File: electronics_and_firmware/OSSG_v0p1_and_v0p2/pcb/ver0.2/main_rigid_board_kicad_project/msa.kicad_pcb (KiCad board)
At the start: 2 copper layers, 47.8 x 9.4 mm, 53 parts, among them J1 USB_B_Micro, J2 SWD Prog, SW1 SW_SPST, U1 MCP1702, U2 MCP73831-2-OT, U3 W25Q128JV, U4 RP2040, U5 ‎DMP21D0UT-7‎, Y1 H130B-12.000-20-3050-EXT-TR

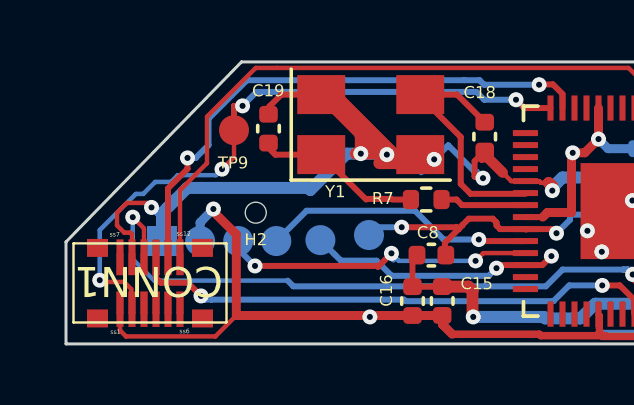
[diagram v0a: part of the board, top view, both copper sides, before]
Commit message: fix MSAv0p2 main board pcb connector pinout, fix gerber renders, update README
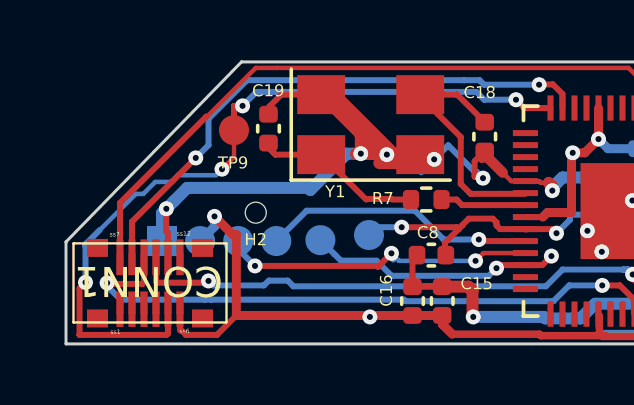
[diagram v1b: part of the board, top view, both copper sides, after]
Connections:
- CONN1 pad 1: +3V3 -> unconnected-(CONN1-Pad1)
- CONN1 pad 10: /MIC_DOUT_2 -> /MIC_DOUT_3
- CONN1 pad 11: /MIC_DOUT_1 -> -BATT
- CONN1 pad 12: /MIC_DOUT_0 -> unconnected-(CONN1-Pad12)
- CONN1 pad 2: /MIC_CLK -> unconnected-(CONN1-Pad2)
- CONN1 pad 5: unconnected-(CONN1-Pad5) -> /MIC_CLK
- CONN1 pad 6: unconnected-(CONN1-Pad6) -> +3V3
- CONN1 pad 7: unconnected-(CONN1-Pad7) -> /MIC_DOUT_0
- CONN1 pad 8: -BATT -> /MIC_DOUT_1
- CONN1 pad 9: /MIC_DOUT_3 -> /MIC_DOUT_2
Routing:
- net /MIC_CLK: track 22.0 -> 25.7 mm
- net /MIC_DOUT_3: track 22.0 -> 18.6 mm
- net -BATT: track 158.9 -> 156.4 mm
- net /MIC_DOUT_2: track 18.6 -> 20.8 mm
- net +3V3: track 113.2 -> 111.2 mm
- net /MIC_DOUT_0: track 21.2 -> 22.0 mm
